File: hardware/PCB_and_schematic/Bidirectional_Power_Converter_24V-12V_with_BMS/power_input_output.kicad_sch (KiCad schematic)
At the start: 17 parts, among them J1 V_IN, J2 V_OUT

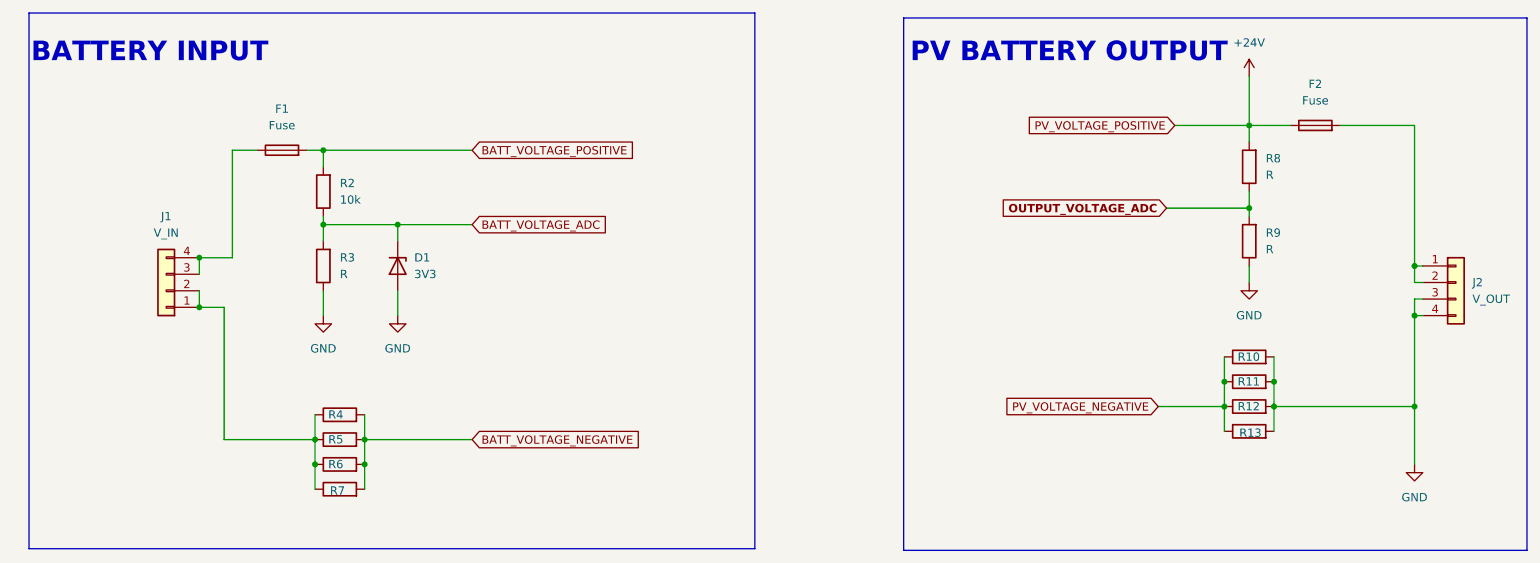
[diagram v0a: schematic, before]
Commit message: Schematic for buck/boost conv
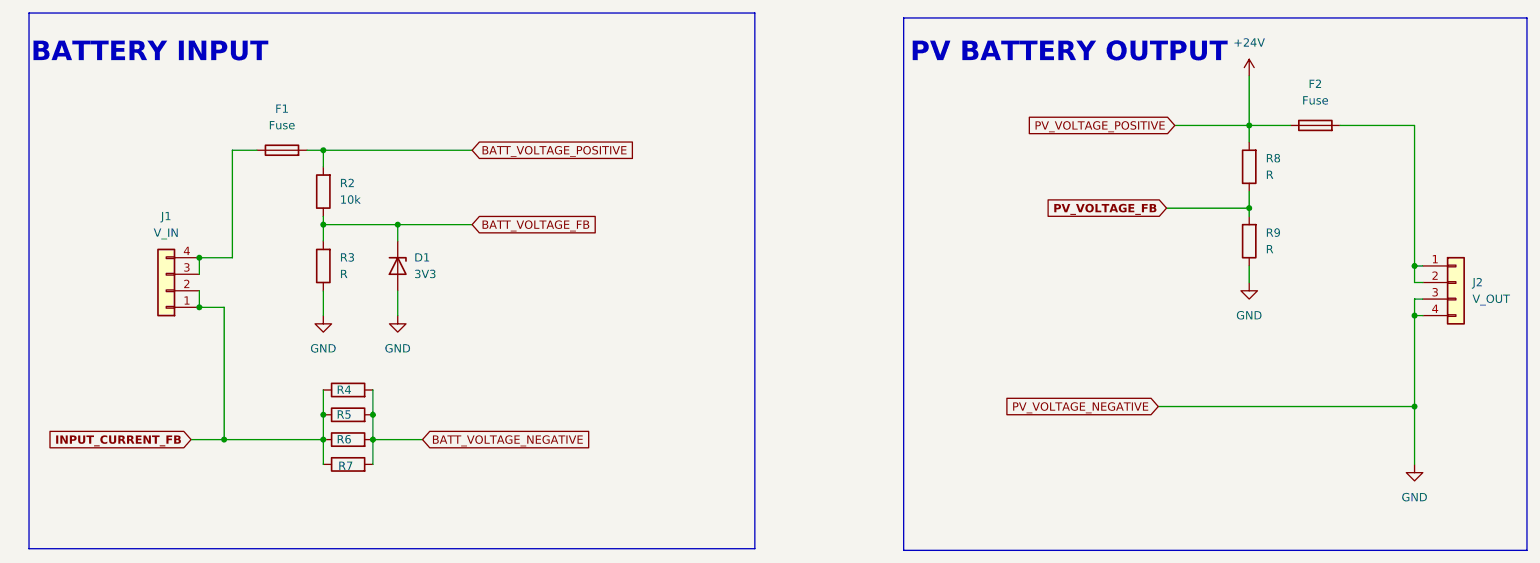
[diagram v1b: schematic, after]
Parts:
- removed R10, R13: 100mR, Resistor_SMD:R_0805_2012Metric, symbol Device:R
- removed R11, R12: R, Resistor_SMD:R_0805_2012Metric, symbol Device:R
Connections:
- net INPUT_CURRENT_FB: now reaches J1.1 (Pin_1), J1.2 (Pin_2), R4.1, R5.1, R6.1, R7.1
- net BATT_VOLTAGE_ADC renamed BATT_VOLTAGE_FB
- net OUTPUT_VOLTAGE_ADC renamed PV_VOLTAGE_FB
